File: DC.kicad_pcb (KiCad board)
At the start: 4 copper layers, 196.5 x 181.5 mm, 86 parts, among them J1 348302001, J2 348302001, J3 757570141, J4 PPTC021LFBN-RC, U6 MCP2551-I-P, U7 NUCLEO-F302R8

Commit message: Change molex orientation
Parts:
- moved J2 50.2 mm to (144.5, 144.5), turned to 0 degrees
- moved J1 49.2 mm to (215.0, 144.5), turned to 0 degrees
- moved S4 0.71 mm to (215.8, 104.0)
- moved R11 0.50 mm to (105.5, 153.0)
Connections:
- U7 pad CN7_16: /+3V3 -> +3.3V
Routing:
- net /HVILActive: track 300.8 -> 1.52 mm, vias 4 -> 1
- net /From_PreChargeBtn: track 176.3 -> 0.00 mm
- net /LVSwitch+: track 234.3 -> 83.1 mm, vias 3 -> 2
- net /HVActive: track 322.4 -> 183.1 mm
- net /ChargeMode: track 138.6 -> 0.00 mm, vias 2 -> 0
- net /DashFaultIndicator: track 300.8 -> 163.1 mm, vias 2 -> 1
- net /LVActive: track 310.5 -> 178.9 mm, vias 4 -> 0
- net /To_PreChargeBtn: track 169.5 -> 44.2 mm, vias 0 -> 1
- net /LVSwitch-: track 205.3 -> 109.7 mm
- net /ThermalShutoff: track 0.00 -> 91.3 mm, vias 0 -> 1
- net /HVSwitch+: track 166.6 -> 76.9 mm, vias 6 -> 0
- net /GreenLED1: track 136.0 -> 46.6 mm, vias 2 -> 0
- net /GreenLED2: track 131.5 -> 43.4 mm, vias 0 -> 2
- net /HVSwitch-: track 189.5 -> 104.5 mm, vias 2 -> 1
- net /AccelIn: track 123.4 -> 40.5 mm
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
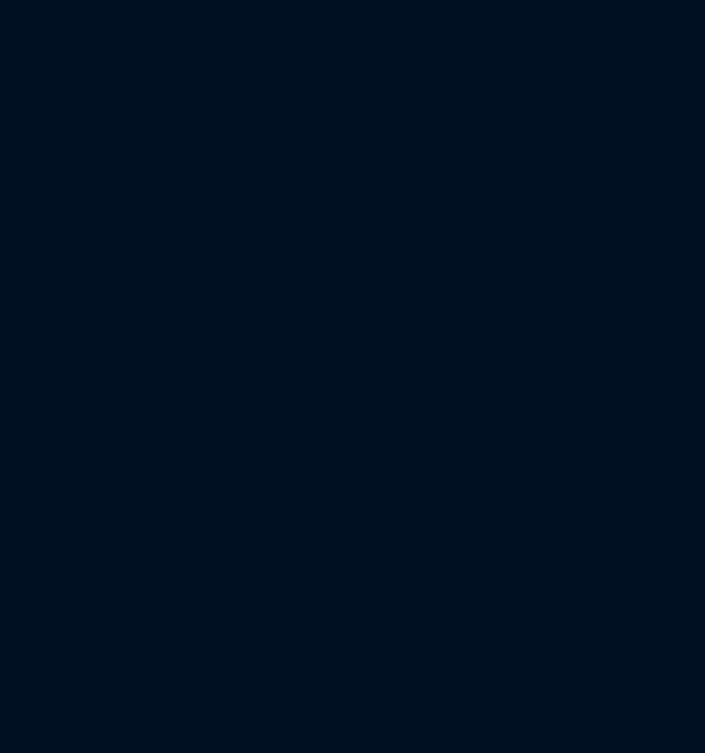
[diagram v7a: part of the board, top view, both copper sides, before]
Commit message: Added gear-select, needs to be wired
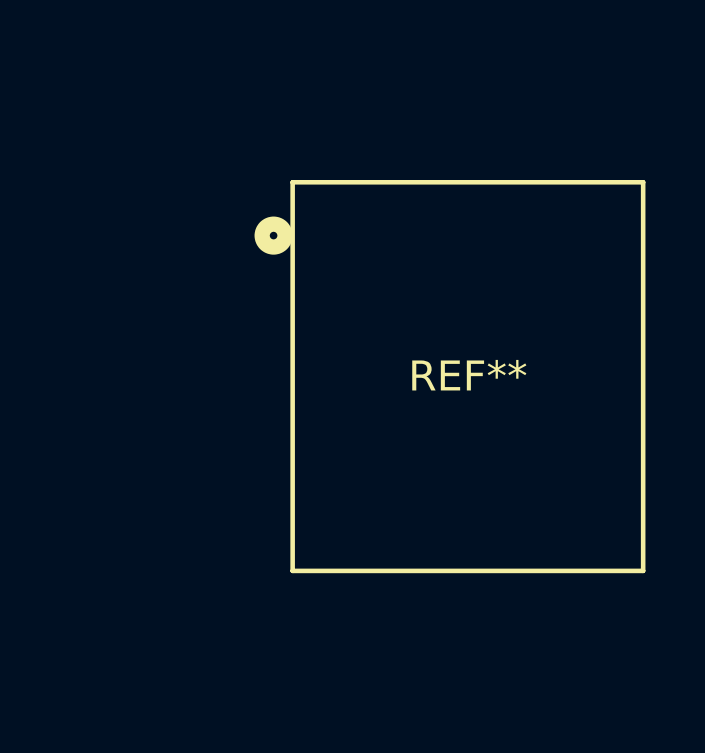
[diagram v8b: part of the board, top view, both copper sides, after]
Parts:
- added REF**: TO_1M1QEH_EWI, MiscellaneousLibrary:TO_1M1QEH_EWI, F.Cu at (285.0, 92.0)
